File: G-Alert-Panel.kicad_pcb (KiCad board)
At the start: 2 copper layers, 234.1 x 93.5 mm, 95 parts, among them SW1 SW_Push, U1 MQ-4b, U2 LM393

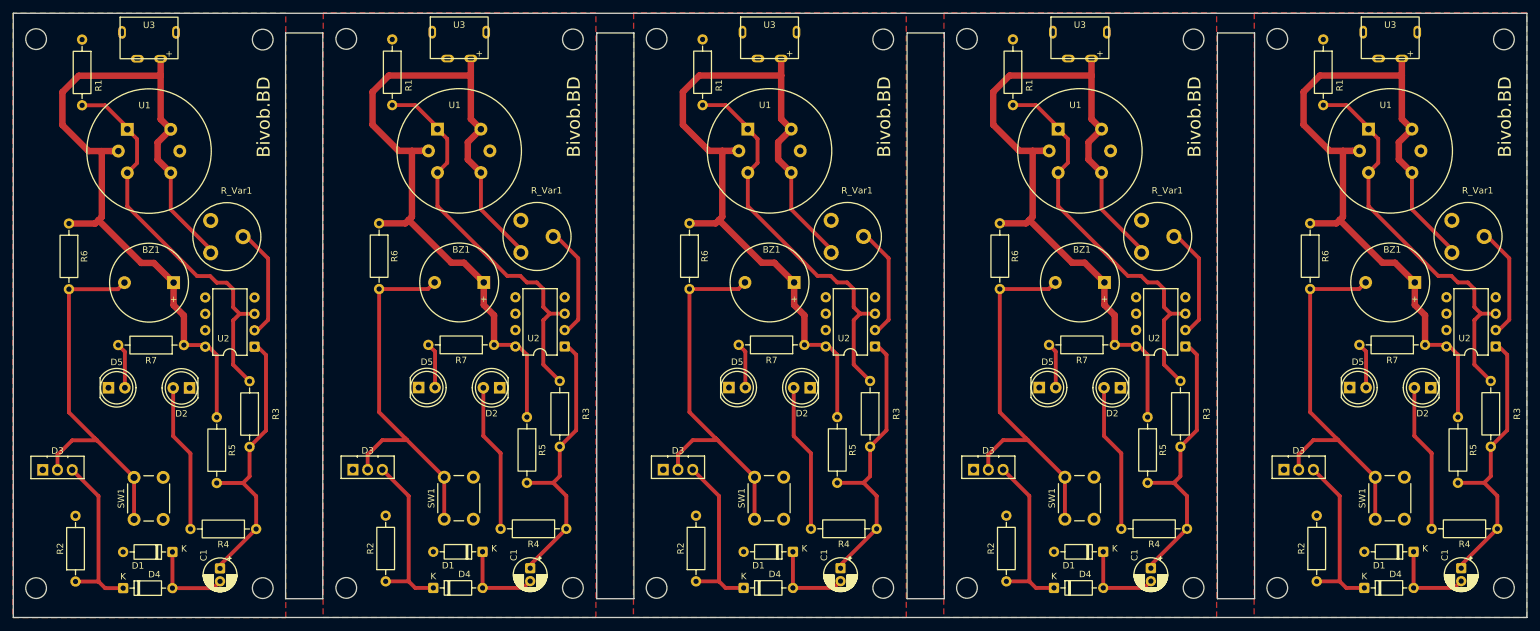
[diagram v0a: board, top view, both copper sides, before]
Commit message: Single Side Correction Update
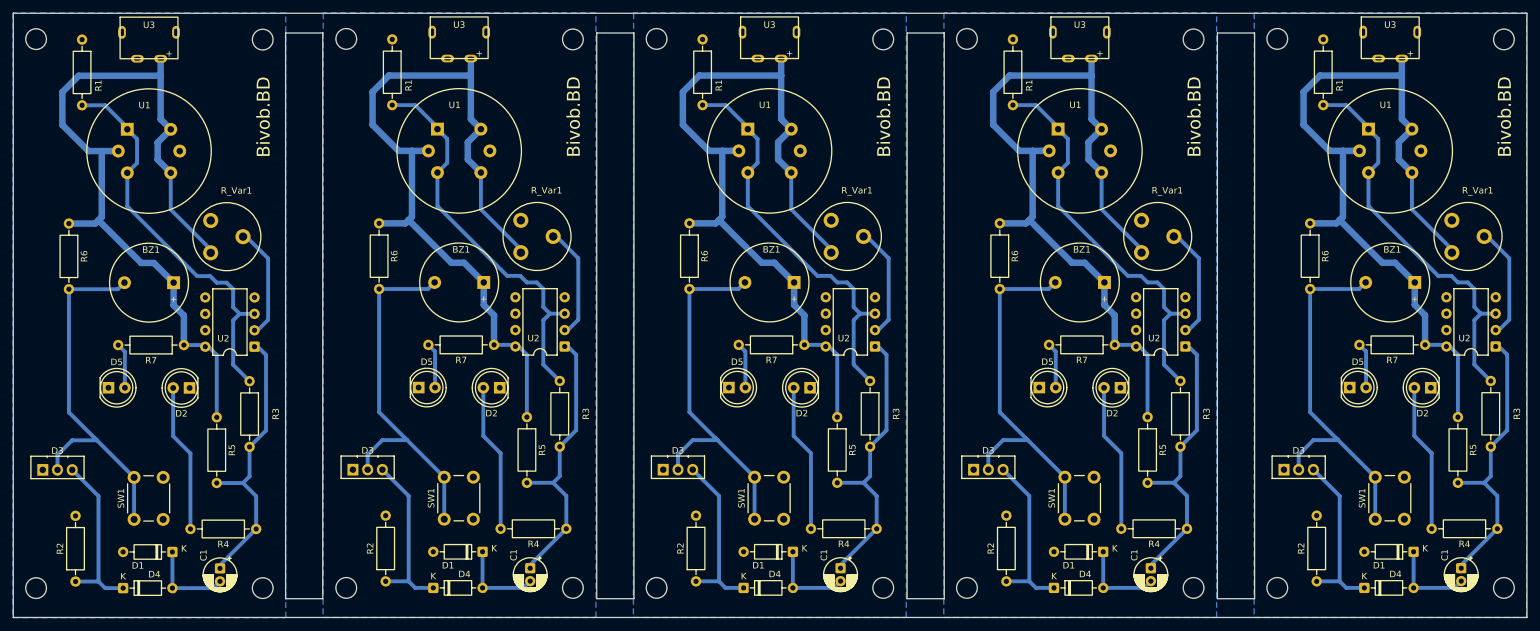
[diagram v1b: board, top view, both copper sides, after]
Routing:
- added copper zone on B.Cu, net GND
- removed copper zone on F.Cu, net GND

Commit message: AC Update with gitignore
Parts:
- removed the BZ1 at (247.7, 98.6)
- removed the BZ1 at (151.7, 98.6)
- removed the BZ1 at (199.7, 98.6)
- removed the C1 at (158.8, 142.8)
- removed the C1 at (206.8, 142.8)
- removed the C1 at (254.8, 142.8)
- removed the D2 at (202.1, 114.9)
- removed the D2 at (154.1, 114.9)
- removed the D2 at (250.1, 114.9)
- removed the D3 at (179.4, 127.5)
- removed the D3 at (227.4, 127.5)
- removed the D3 at (131.4, 127.5)
- removed the D5 at (237.6, 114.8)
- removed the D5 at (141.6, 114.8)
- removed the D5 at (189.6, 114.8)
- removed the R1 at (233.5, 61.0)
- removed the R1 at (137.5, 61.0)
- removed the R1 at (185.5, 61.0)
- removed the R2 at (136.5, 144.8)
- removed the R2 at (232.5, 144.8)
- removed the R2 at (184.5, 144.8)
- removed the R3 at (259.4, 113.8)
- removed the R3 at (211.4, 113.8)
- removed the R3 at (163.4, 113.8)
- removed the R4 at (260.4, 136.7)
- removed the R4 at (212.4, 136.7)
- removed the R4 at (164.4, 136.7)
- removed the R5 at (254.3, 119.4)
- removed the R5 at (206.3, 119.4)
- removed the R5 at (158.3, 119.4)
- removed the R6 at (135.5, 89.4)
- removed the R6 at (231.5, 89.4)
- removed the R6 at (183.5, 89.4)
- removed the R7 at (201.2, 108.2)
- removed the R7 at (153.2, 108.2)
- removed the R7 at (249.2, 108.2)
- removed the R_Var1 at (205.4, 94.0)
- removed the R_Var1 at (157.4, 94.0)
- removed the R_Var1 at (253.4, 94.0)
- removed the SW1 at (193.5, 135.2)
- removed the SW1 at (145.5, 135.2)
- removed the SW1 at (241.5, 135.2)
- removed the U1 at (240.5, 74.9)
- removed the U1 at (144.5, 74.9)
- removed the U1 at (192.5, 74.9)
- removed the U2 at (164.2, 108.5)
- removed the U2 at (212.2, 108.5)
- removed the U2 at (260.2, 108.5)
- removed the U3 at (195.9, 59.9)
- removed the U3 at (147.9, 59.9)
- removed the U3 at (243.9, 59.9)
- added BZ1: Buzzer, Buzzer_Beeper:Buzzer_12x9.5RM7.6, F.Cu at (195.9, 94.0)
- added BZ1: Buzzer, Buzzer_Beeper:Buzzer_12x9.5RM7.6, F.Cu at (147.9, 94.0)
- added BZ1: Buzzer, Buzzer_Beeper:Buzzer_12x9.5RM7.6, F.Cu at (243.9, 94.0)
- added C1: 10uF, Capacitor_THT:CP_Radial_D5.0mm_P2.00mm, F.Cu at (210.2, 131.8)
- added C1: 10uF, Capacitor_THT:CP_Radial_D5.0mm_P2.00mm, F.Cu at (258.2, 131.8)
- added C1: 10uF, Capacitor_THT:CP_Radial_D5.0mm_P2.00mm, F.Cu at (162.2, 131.8)
- added D2: LED, LED_THT:LED_D5.0mm, F.Cu at (141.6, 115.0)
- added D2: LED, LED_THT:LED_D5.0mm, F.Cu at (189.6, 115.0)
- added D2: LED, LED_THT:LED_D5.0mm, F.Cu at (237.6, 115.0)
- added D3: NEC24PM, Package_TO_SOT_THT:TO-126-3_Vertical, F.Cu at (136.8, 120.2)
- added D3: NEC24PM, Package_TO_SOT_THT:TO-126-3_Vertical, F.Cu at (184.8, 120.2)
- added D3: NEC24PM, Package_TO_SOT_THT:TO-126-3_Vertical, F.Cu at (232.8, 120.2)
- added D5: LED, LED_THT:LED_D5.0mm, F.Cu at (247.6, 115.0)
- added D5: LED, LED_THT:LED_D5.0mm, F.Cu at (199.6, 115.0)
- added D5: LED, LED_THT:LED_D5.0mm, F.Cu at (151.6, 115.0)
- added R1: 5.1k, Resistor_THT:R_Axial_DIN0207_L6.3mm_D2.5mm_P10.16mm_Horizontal, F.Cu at (181.8, 69.7)
- added R1: 5.1k, Resistor_THT:R_Axial_DIN0207_L6.3mm_D2.5mm_P10.16mm_Horizontal, F.Cu at (133.8, 69.7)
- added R1: 5.1k, Resistor_THT:R_Axial_DIN0207_L6.3mm_D2.5mm_P10.16mm_Horizontal, F.Cu at (229.8, 69.7)
- added R2: 1k, Resistor_THT:R_Axial_DIN0207_L6.3mm_D2.5mm_P10.16mm_Horizontal, F.Cu at (233.0, 139.3)
- added R2: 1k, Resistor_THT:R_Axial_DIN0207_L6.3mm_D2.5mm_P10.16mm_Horizontal, F.Cu at (185.0, 139.3)
- added R2: 1k, Resistor_THT:R_Axial_DIN0207_L6.3mm_D2.5mm_P10.16mm_Horizontal, F.Cu at (137.0, 139.3)
- added R3: 1.5M, Resistor_THT:R_Axial_DIN0207_L6.3mm_D2.5mm_P10.16mm_Horizontal, F.Cu at (140.7, 107.8)
- added R3: 1.5M, Resistor_THT:R_Axial_DIN0207_L6.3mm_D2.5mm_P10.16mm_Horizontal, F.Cu at (188.7, 107.8)
- added R3: 1.5M, Resistor_THT:R_Axial_DIN0207_L6.3mm_D2.5mm_P10.16mm_Horizontal, F.Cu at (236.7, 107.8)
- added R4: 1k, Resistor_THT:R_Axial_DIN0207_L6.3mm_D2.5mm_P10.16mm_Horizontal, F.Cu at (255.6, 123.2)
- added R4: 1k, Resistor_THT:R_Axial_DIN0207_L6.3mm_D2.5mm_P10.16mm_Horizontal, F.Cu at (159.6, 123.2)
- added R4: 1k, Resistor_THT:R_Axial_DIN0207_L6.3mm_D2.5mm_P10.16mm_Horizontal, F.Cu at (207.6, 123.2)
- added R5: 4.7k, Resistor_THT:R_Axial_DIN0207_L6.3mm_D2.5mm_P10.16mm_Horizontal, F.Cu at (260.0, 124.8)
- added R5: 4.7k, Resistor_THT:R_Axial_DIN0207_L6.3mm_D2.5mm_P10.16mm_Horizontal, F.Cu at (212.0, 124.8)
- added R5: 4.7k, Resistor_THT:R_Axial_DIN0207_L6.3mm_D2.5mm_P10.16mm_Horizontal, F.Cu at (164.0, 124.8)
- added R6: 1k, Resistor_THT:R_Axial_DIN0207_L6.3mm_D2.5mm_P10.16mm_Horizontal, F.Cu at (183.8, 86.9)
- added R6: 1k, Resistor_THT:R_Axial_DIN0207_L6.3mm_D2.5mm_P10.16mm_Horizontal, F.Cu at (135.8, 86.9)
- added R6: 1k, Resistor_THT:R_Axial_DIN0207_L6.3mm_D2.5mm_P10.16mm_Horizontal, F.Cu at (231.8, 86.9)
- added R7: 1k, Resistor_THT:R_Axial_DIN0207_L6.3mm_D2.5mm_P10.16mm_Horizontal, F.Cu at (156.0, 141.3)
- added R7: 1k, Resistor_THT:R_Axial_DIN0207_L6.3mm_D2.5mm_P10.16mm_Horizontal, F.Cu at (204.0, 141.3)
- added R7: 1k, Resistor_THT:R_Axial_DIN0207_L6.3mm_D2.5mm_P10.16mm_Horizontal, F.Cu at (252.0, 141.3)
- added R_Var1: 10k, Potentiometer_THT:Potentiometer_Piher_PT-10-V05_Vertical, F.Cu at (162.8, 88.5)
- added R_Var1: 10k, Potentiometer_THT:Potentiometer_Piher_PT-10-V05_Vertical, F.Cu at (258.8, 88.5)
- added R_Var1: 10k, Potentiometer_THT:Potentiometer_Piher_PT-10-V05_Vertical, F.Cu at (210.8, 88.5)
- added SW1: SW_Push, Button_Switch_THT:SW_PUSH_6mm, F.Cu at (246.2, 128.5)
- added SW1: SW_Push, Button_Switch_THT:SW_PUSH_6mm, F.Cu at (198.2, 128.5)
- added SW1: SW_Push, Button_Switch_THT:SW_PUSH_6mm, F.Cu at (150.2, 128.5)
- added U1: MQ-4b, Sensor:MQ-6, F.Cu at (240.6, 74.9)
- added U1: MQ-4b, Sensor:MQ-6, F.Cu at (192.6, 74.9)
- added U1: MQ-4b, Sensor:MQ-6, F.Cu at (144.6, 74.9)
- added U2: LM393, Package_DIP:DIP-8_W7.62mm, F.Cu at (204.5, 100.8)
- added U2: LM393, Package_DIP:DIP-8_W7.62mm, F.Cu at (156.5, 100.8)
- added U2: LM393, Package_DIP:DIP-8_W7.62mm, F.Cu at (252.5, 100.8)
- added U3: ~, USB-C Connector:USB-C, F.Cu at (147.9, 59.9)
- added U3: ~, USB-C Connector:USB-C, F.Cu at (195.9, 59.9)
- added U3: ~, USB-C Connector:USB-C, F.Cu at (243.9, 59.9)
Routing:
- net Net-(U1-B1): track 309.7 -> 383.8 mm
- net Net-(BZ1--): track 292.5 -> 333.9 mm
- net Net-(D2-A): track 114.6 -> 79.6 mm
- net Net-(D5-A): track 35.2 -> 66.7 mm
- net +5V: track 618.8 -> 646.8 mm
- net Net-(C1-Pad1): track 217.6 -> 241.5 mm
- net Net-(D3-G): track 133.7 -> 157.3 mm
- net Net-(D1-K): track 71.3 -> 88.3 mm
- net Net-(U2A--): track 85.2 -> 81.3 mm
- net GND: track 0.00 -> 1.08 mm
